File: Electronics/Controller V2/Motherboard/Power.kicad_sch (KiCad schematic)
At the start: 28 parts, among them J14 TABLET 1 PWR, J15 TABLET 2 PWR, U10 LM2587S-ADJ/NOPB, U8 LM2596S-5, U9 LM2587S-ADJ/NOPB

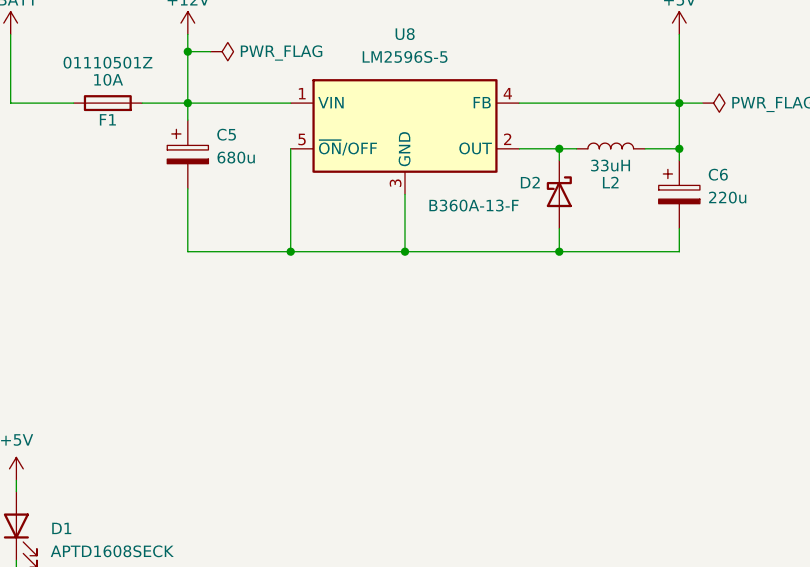
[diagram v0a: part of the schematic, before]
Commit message: Added missing ground connection. Working on PCB layout.
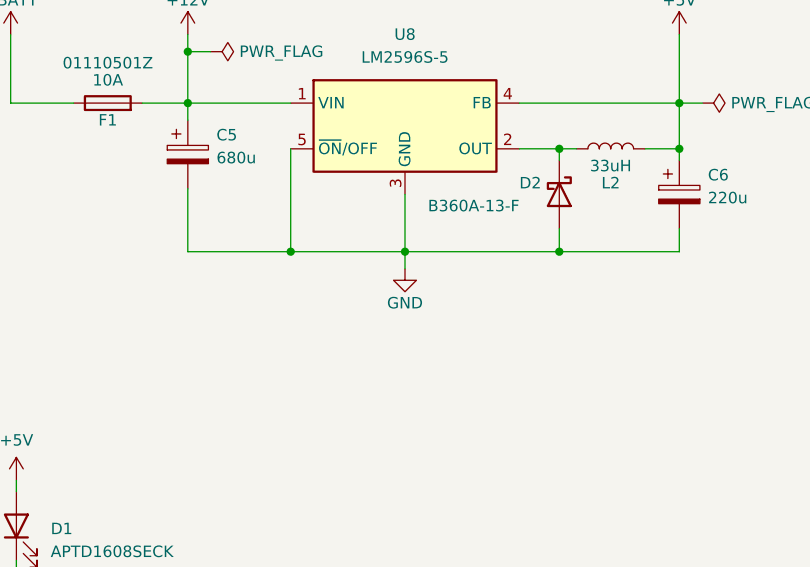
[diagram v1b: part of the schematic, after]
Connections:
- net GND: now also C5.2, C6.2, D2.2 (A), U8.3 (GND), U8.5 (~{ON}/OFF)
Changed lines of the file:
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@@
   (title_block
     (title "Tandem Leveller Controller")
-    (date "2026-02-02")
+    (date "2026-02-06")
     (rev "V2.0")
     (company "(C) andy@britishideas.com 2026")
@@
   )
   (wire (pts (xy 194.945 106.68) (xy 191.77 106.68))
+    (stroke (width 0) (type default))
+  )
+  (wire (pts (xy 104.775 106.045) (xy 104.775 107.95))
     (stroke (width 0) (type default))
   )
@@
         )
       )
+    )
+  )
+  (symbol (lib_id "power:GND") (at 104.775 107.95 0) (unit 1)
+    (in_bom yes) (on_board yes) (dnp no)
+    (property "Reference" "#PWR039" (at 104.775 114.3 0)
+      (effects (font (size 1.27 1.27)) hide)
+    )
+    (property "Value" "GND" (at 104.775 111.76 0)
+      (effects (font (size 1.27 1.27)))
+    )
+    (property "Footprint" "" (at 104.775 107.95 0)
+      (effects (font (size 1.27 1.27)) hide)
+    )
+    (property "Datasheet" "" (at 104.775 107.95 0)
+      (effects (font (size 1.27 1.27)) hide)
+    )
+    (pin "1")
+    (instances
+      (project "Tandem Leveller Controller V2"
+        (path "/dceffac9-8f5b-4889-8265-b6c471cb5dde/c704cbc6-3202-48f7-92de-057996cf69f8"
+          (reference "#PWR039") (unit 1)
+        )
+      )

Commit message: IMU code tested and working.
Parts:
- C7, C8: value 1729034 -> 100u
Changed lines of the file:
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@@
       (effects (font (size 1.27 1.27)) (justify left))
     )
-    (property "Value" "1729034" (at 170.18 115.951 0)
+    (property "Value" "100u" (at 170.18 115.951 0)
       (effects (font (size 1.27 1.27)) (justify left))
     )
@@
       (effects (font (size 1.27 1.27)) (justify left))
     )
-    (property "Value" "1729034" (at 170.18 59.436 0)
+    (property "Value" "100u" (at 170.18 59.436 0)
       (effects (font (size 1.27 1.27)) (justify left))
     )
